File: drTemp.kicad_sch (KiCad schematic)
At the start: 21 parts, among them U1 STM32F411CEU6, U2 AZ1084CD-3.3TRG1, U3 MX950T-9.5-02P-GN01-CU-PS-A, U4 SE5218ALG-LF, X1 TAXM8M4RDBCCT2T

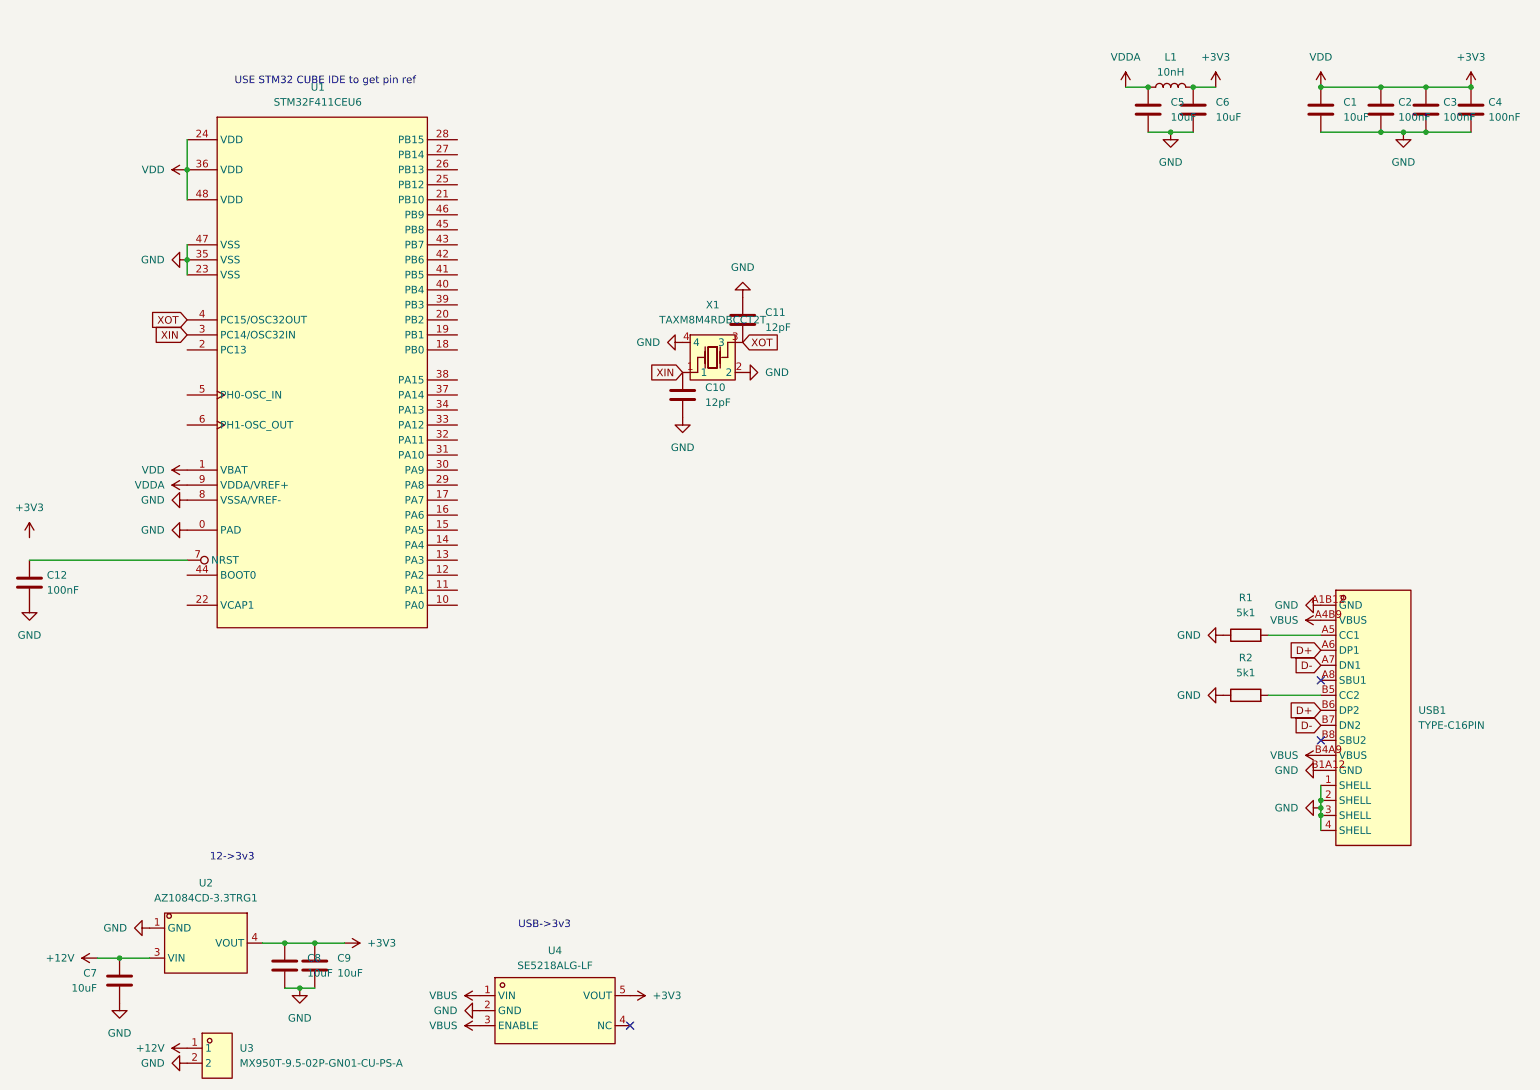
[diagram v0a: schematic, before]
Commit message: nearly done with schematic, every pin is being used
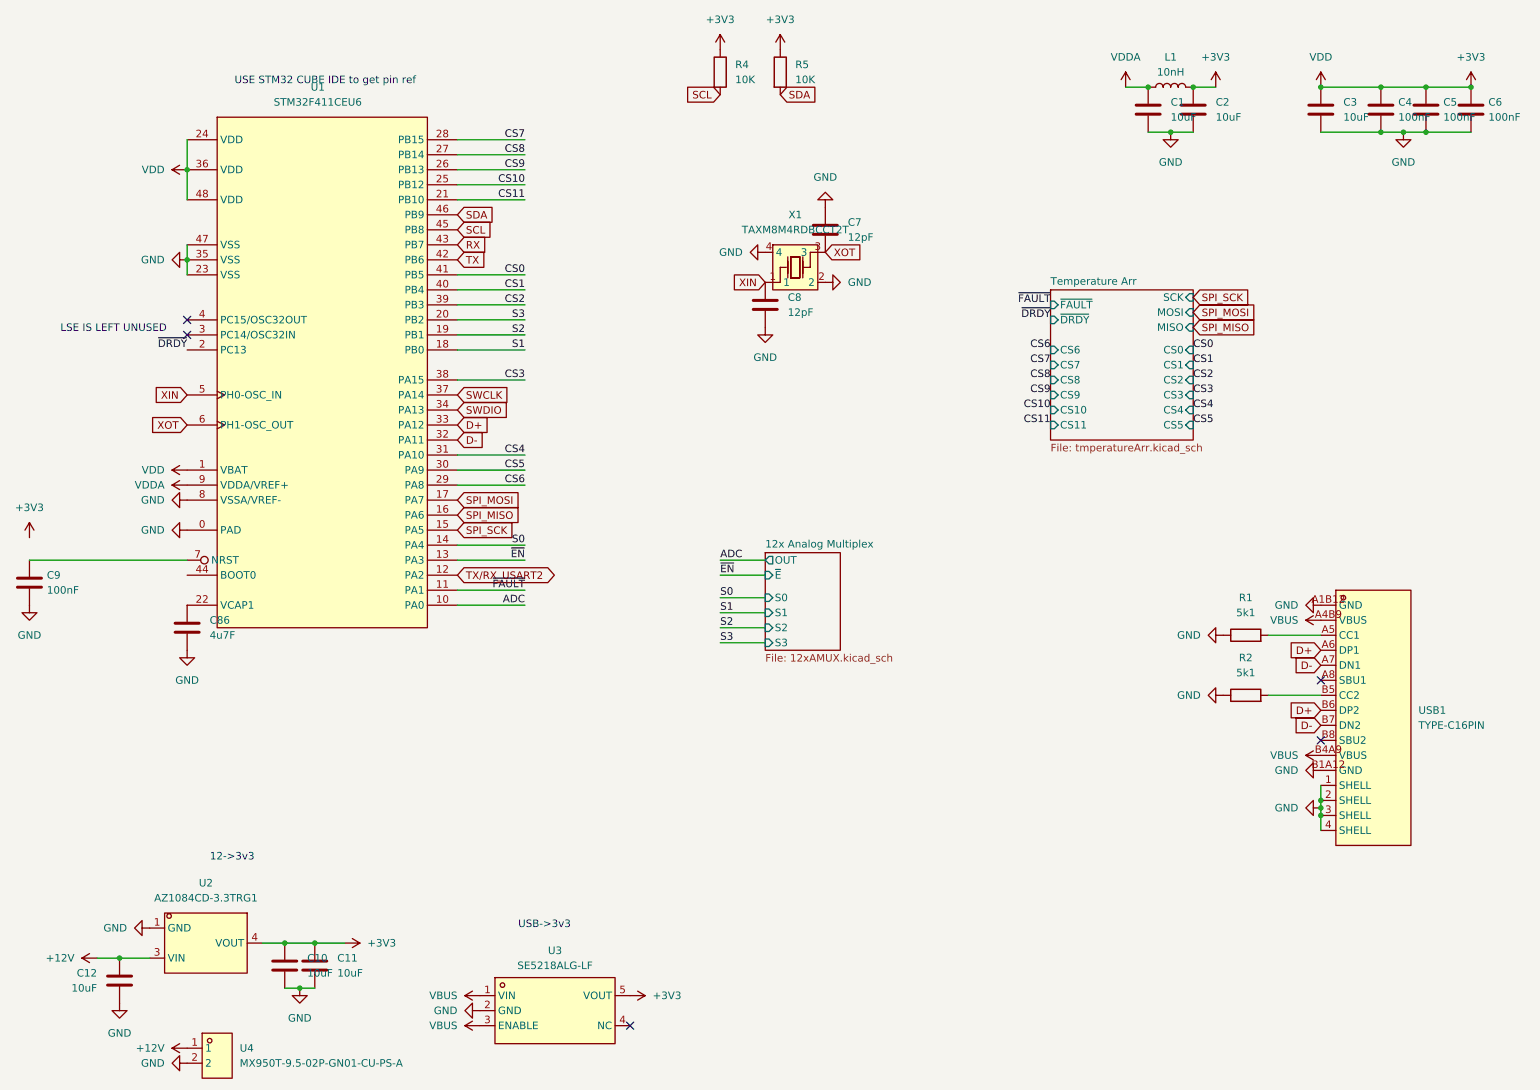
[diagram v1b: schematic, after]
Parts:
- added C86: 4u7F, Capacitor_SMD:C_0402_1005Metric, symbol Device:C
- added R4, R5: 10K, Resistor_SMD:R_0603_1608Metric, symbol Device:R
- C1: renamed from C5; footprint (none) -> Capacitor_SMD:C_0402_1005Metric
- C10: renamed from C8; footprint (none) -> Capacitor_SMD:C_0402_1005Metric
- C11: renamed from C9; footprint (none) -> Capacitor_SMD:C_0402_1005Metric
- C12: renamed from C7; footprint (none) -> Capacitor_SMD:C_0402_1005Metric
- C2: renamed from C6; footprint (none) -> Capacitor_SMD:C_0402_1005Metric
- C3: renamed from C1; footprint (none) -> Capacitor_SMD:C_0402_1005Metric
- C4: renamed from C2; footprint (none) -> Capacitor_SMD:C_0402_1005Metric
- C5: renamed from C3; footprint (none) -> Capacitor_SMD:C_0402_1005Metric
- C6: renamed from C4; footprint (none) -> Capacitor_SMD:C_0402_1005Metric
- C7: renamed from C11; footprint (none) -> Capacitor_SMD:C_0402_1005Metric
- C8: renamed from C10; footprint (none) -> Capacitor_SMD:C_0402_1005Metric
- C9: renamed from C12; footprint (none) -> Capacitor_SMD:C_0402_1005Metric
- L1: footprint (none) -> Capacitor_SMD:C_0402_1005Metric
- R1, R2: footprint (none) -> Resistor_SMD:R_0603_1608Metric
- renumbered U4 to U3, U3 to U4
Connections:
- net +3V3: now also R4.1, R5.1
- net D+: now also U1.33 (PA12)
- net D-: now also U1.32 (PA11)
- net GND: now also C86.2
- net XIN: now also U1.5 (PH0-OSC_IN); no longer U1.3 (PC14/OSC32IN)
- net XOT: now also U1.6 (PH1-OSC_OUT); no longer U1.4 (PC15/OSC32OUT)
- net ADC: now reaches U1.10 (PA0)
- net ~{FAULT}: now reaches U1.11 (PA1)
- net TX/RX_USART2: now reaches U1.12 (PA2)
- net ~{EN}: now reaches U1.13 (PA3)
- net S0: now reaches U1.14 (PA4)
- net SPI_SCK: now reaches U1.15 (PA5)
- net SPI_MISO: now reaches U1.16 (PA6)
- net SPI_MOSI: now reaches U1.17 (PA7)
- net S1: now reaches U1.18 (PB0)
- net S2: now reaches U1.19 (PB1)
- net ~{DRDY}: now reaches U1.2 (PC13)
- net S3: now reaches U1.20 (PB2)
- net CS11: now reaches U1.21 (PB10)
- net at U1.22 (VCAP1): now also C86.1
- net CS10: now reaches U1.25 (PB12)
- net CS9: now reaches U1.26 (PB13)
- net CS8: now reaches U1.27 (PB14)
- net CS7: now reaches U1.28 (PB15)
- net CS6: now reaches U1.29 (PA8)
- net CS5: now reaches U1.30 (PA9)
- net CS4: now reaches U1.31 (PA10)
- net SWDIO: now reaches U1.34 (PA13)
- net SWCLK: now reaches U1.37 (PA14)
- net CS3: now reaches U1.38 (PA15)
- net CS2: now reaches U1.39 (PB3)
- net CS1: now reaches U1.40 (PB4)
- net CS0: now reaches U1.41 (PB5)
- net TX: now reaches U1.42 (PB6)
- net RX: now reaches U1.43 (PB7)
- net SCL: now reaches U1.45 (PB8)
- net SCL: now also R4.2
- net SDA: now reaches U1.46 (PB9)
- net SDA: now also R5.2
- no-connect marks 3 -> 5
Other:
- added sheet 12x Analog Multiplex (12xAMUX.kicad_sch)
- added sheet Temperature Arr (tmperatureArr.kicad_sch)
- note added: "LSE IS LEFT UNUSED"
- moved on the sheet: C7, C8, X1
